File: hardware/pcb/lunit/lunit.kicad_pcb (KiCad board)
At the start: 4 copper layers, 62.2 x 21.6 mm, 41 parts, among them J1 BUS, J2 Input A, J3 Input B, J4 Control, J5 Flags, J6 Power, U7 74HC245, U8 74HC125

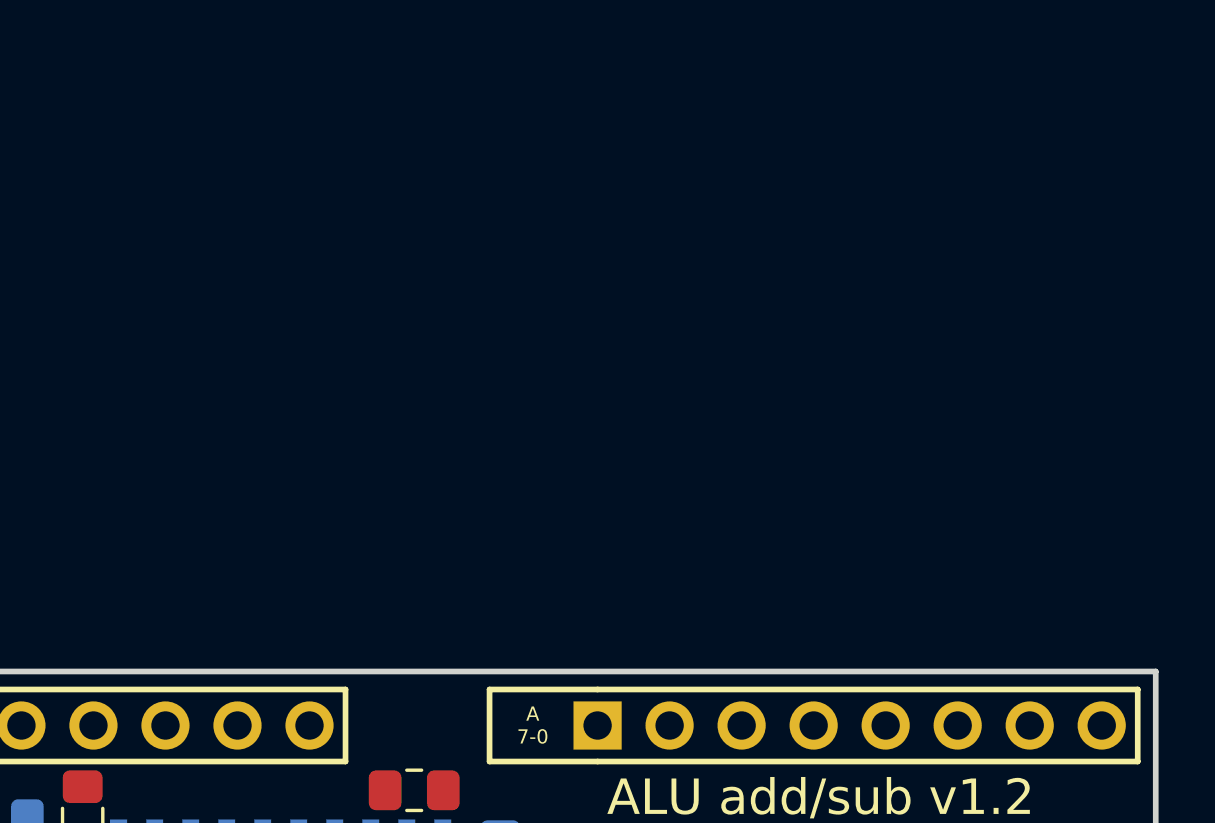
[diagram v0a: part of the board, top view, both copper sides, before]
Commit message: Add And/Or/Sel chips
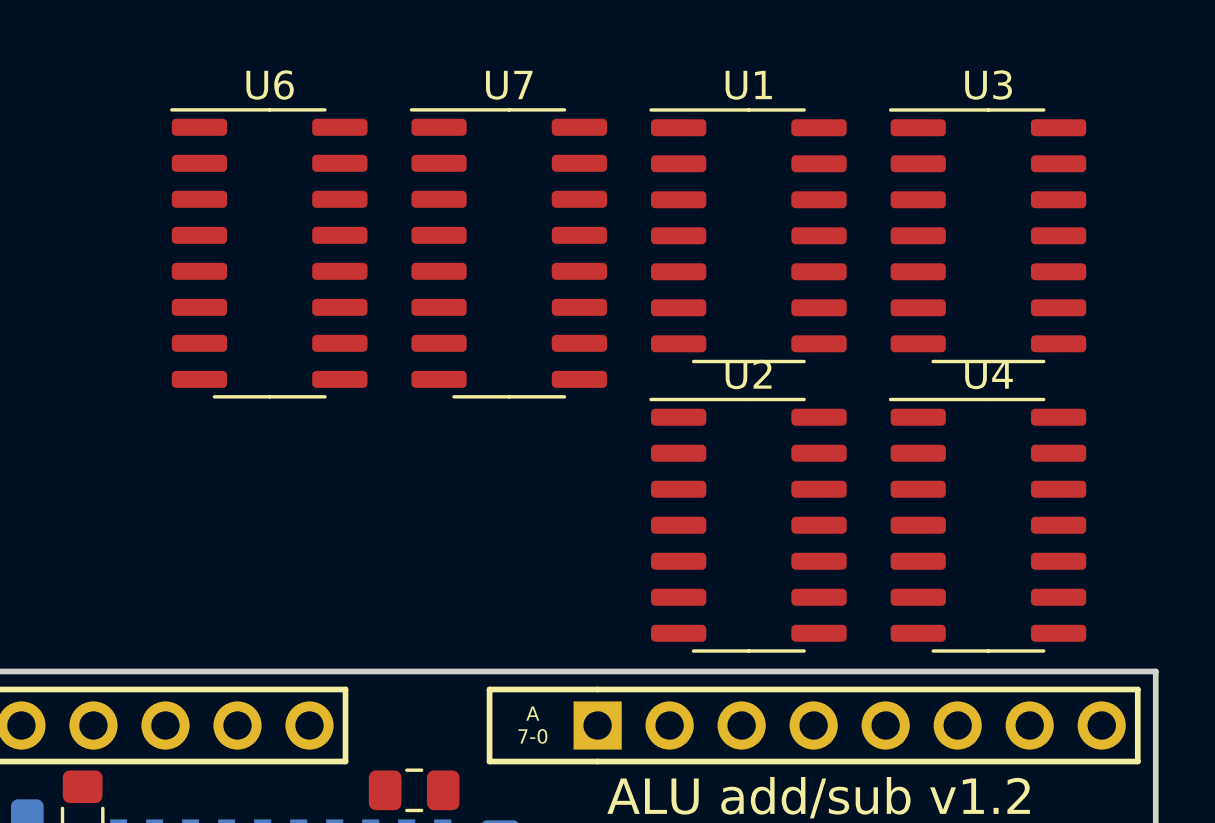
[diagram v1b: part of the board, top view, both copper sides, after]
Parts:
- added U1: 74HC08, Package_SO:SOIC-14_3.9x8.7mm_P1.27mm, F.Cu at (82.8, 20.8)
- added U2: 74HC08, Package_SO:SOIC-14_3.9x8.7mm_P1.27mm, F.Cu at (82.8, 31.0)
- added U3: 74HC32, Package_SO:SOIC-14_3.9x8.7mm_P1.27mm, F.Cu at (91.3, 20.8)
- added U4: 74HC32, Package_SO:SOIC-14_3.9x8.7mm_P1.27mm, F.Cu at (91.3, 31.0)
- added U6: 74HC157, Package_SO:SOIC-16_3.9x9.9mm_P1.27mm, F.Cu at (65.9, 21.4)
- added U7: 74HC157, Package_SO:SOIC-16_3.9x9.9mm_P1.27mm, F.Cu at (74.4, 21.4)
- renumbered D0 to D1, D11 to D10, D12 to D11, D1 to D2, D2 to D3, D3 to D4, D4 to D5, D5 to D6, D6 to D7, D7 to D8, D8 to D9, J6 to J1, J4 to J2, J1 to J3, J2 to J4, J3 to J6, R0 to R1, R11 to R10, R14 to R11, R1 to R2, R2 to R3, R3 to R4, R4 to R5, R5 to R6, R6 to R7, R7 to R8, R8 to R9, U8 to U5, U7 to U8
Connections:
- net ADD_SUB renamed AND_OR
- J4 pad 1: (no net) -> A7
- J4 pad 2: (no net) -> A6
- J4 pad 3: (no net) -> A5
- J4 pad 4: (no net) -> A4
- J4 pad 5: (no net) -> A3
- J4 pad 6: (no net) -> A2
- J4 pad 7: (no net) -> A1
- J4 pad 8: (no net) -> A0
- J6 pad 1: (no net) -> B7
- J6 pad 2: (no net) -> B6
- J6 pad 3: (no net) -> B5
- J6 pad 4: (no net) -> B4
- J6 pad 5: (no net) -> B3
- J6 pad 6: (no net) -> B2
- J6 pad 7: (no net) -> B1
- J6 pad 8: (no net) -> B0

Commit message: Place the chips
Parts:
- D10: value SUB -> OR
- U3, U4: moved to B.Cu
- moved U3 27.8 mm to (80.3, 46.4)
- moved U1 25.6 mm to (80.4, 46.4), turned to 180 degrees
- moved U6 24.8 mm to (55.9, 44.1), turned to 90 degrees
- moved U7 23.3 mm to (69.1, 44.1), turned to 90 degrees
- moved U2 17.3 mm to (90.9, 46.4), turned to 180 degrees
- moved U4 15.3 mm to (90.9, 46.4)
- moved C6 9.71 mm to (49.7, 42.3)
- moved C8 8.36 mm to (62.9, 42.3), turned to 270 degrees
- moved D3 2.03 mm to (66.8, 50.7)
- moved D11 2.03 mm to (52.8, 50.7)
- moved D4 2.03 mm to (64.9, 50.7)
- moved D6 2.03 mm to (61.1, 50.7)
- moved D7 2.03 mm to (59.2, 50.7)
- moved D8 2.03 mm to (57.3, 50.7)
- moved D1 2.03 mm to (70.6, 50.7)
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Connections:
- net SUM0 renamed RES0
- net SUM1 renamed RES1
- net SUM2 renamed RES2
- net SUM3 renamed RES3
- net SUM4 renamed RES4
- net SUM5 renamed RES5
- net SUM6 renamed RES6
- net SUM7 renamed RES7
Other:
- board text added: "/ / / Z"
- board text added: "ALU and/or v1.0"
- board text removed: "6502"
- board text removed: "ALU add/sub v1.2"
- board text removed: "CI V CO Z"
- board text removed: "Z80"

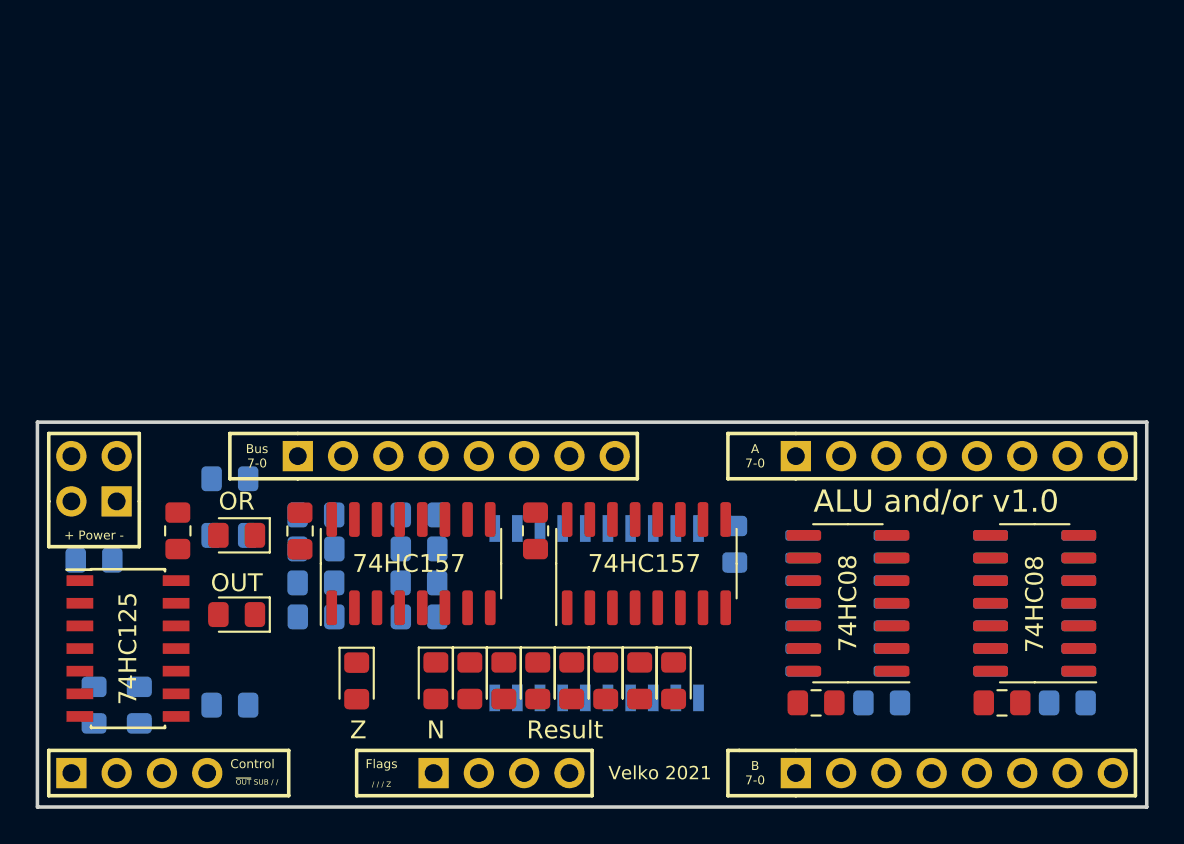
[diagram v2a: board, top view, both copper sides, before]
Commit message: Routed function part
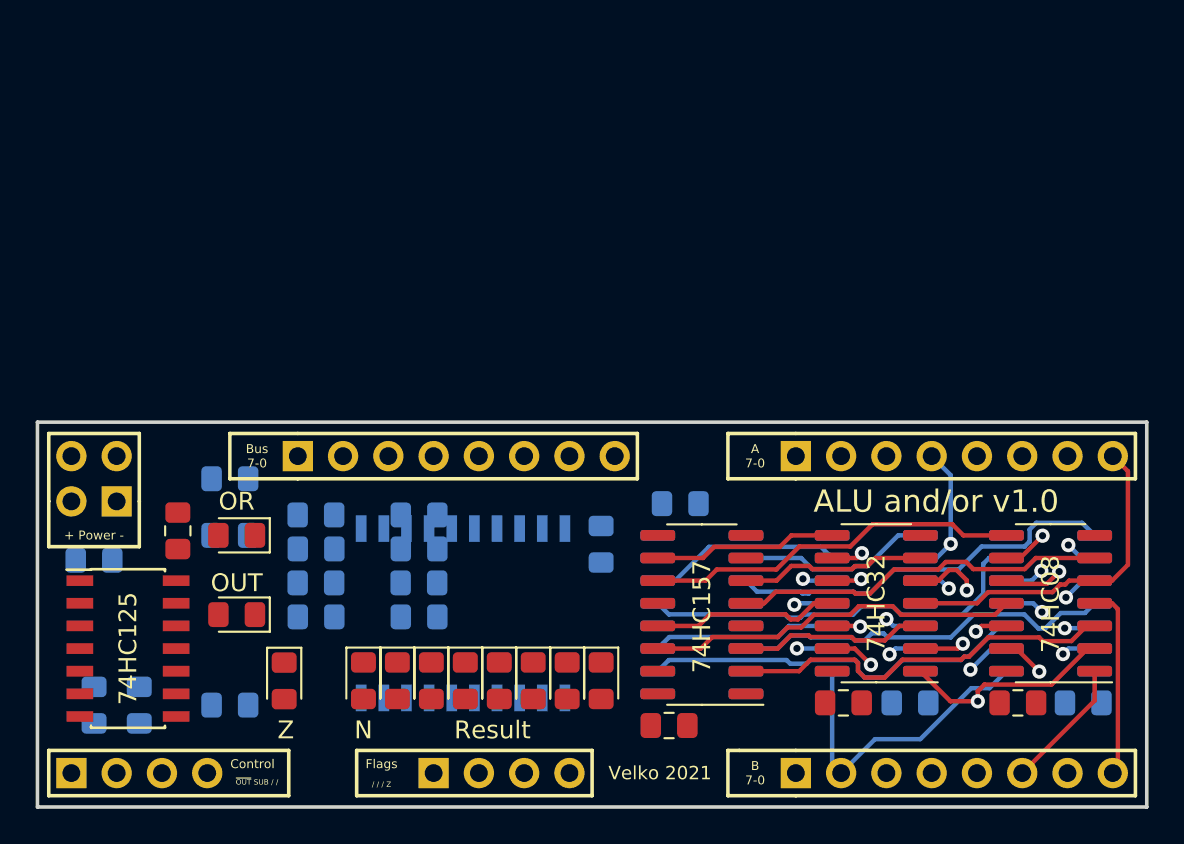
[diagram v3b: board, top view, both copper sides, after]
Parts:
- C6, U1, U6: moved to B.Cu
- U4: moved to F.Cu
- moved C6 21.4 mm to (71.0, 40.8), turned to 0 degrees
- moved U6 16.6 mm to (72.2, 47.0), turned to 180 degrees
- moved C8 13.2 mm to (70.4, 53.2), turned to 0 degrees
- moved U3 11.4 mm to (91.8, 46.4)
- moved U4 8.89 mm to (82.0, 46.4), turned to 180 degrees
- moved C2 7.49 mm to (66.5, 43.0)
- moved U8 7.49 mm to (58.8, 46.9)
- moved U7 4.22 mm to (72.2, 47.0), turned to 180 degrees
- moved D3 4.06 mm to (62.7, 50.7)
- moved D4 4.06 mm to (60.8, 50.7)
- moved D11 4.06 mm to (48.8, 50.7)
- moved D5 4.06 mm to (58.9, 50.7)
- moved D6 4.06 mm to (57.0, 50.7)
- moved D7 4.06 mm to (55.1, 50.7)
- moved D8 4.06 mm to (53.2, 50.7)
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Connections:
- J2 pad 3: (no net) -> Net-(J2-Pad3)
- J2 pad 4: (no net) -> Net-(J2-Pad4)
- J5 pad 1: (no net) -> Net-(J5-Pad1)
- J5 pad 2: (no net) -> Net-(J5-Pad2)
- J5 pad 3: (no net) -> Net-(J5-Pad3)
- U1 pad 1: A7 -> B6
- U1 pad 10: B5 -> B4
- U1 pad 11: AND4 -> AND5
- U1 pad 12: A4 -> A5
- U1 pad 13: B4 -> B5
- U1 pad 2: B7 -> A6
- U1 pad 3: AND7 -> AND6
- U1 pad 4: A6 -> B7
- U1 pad 5: B6 -> A7
- U1 pad 6: AND6 -> AND7
- U1 pad 8: AND5 -> AND4
- U1 pad 9: A5 -> A4
- U2 pad 1: A3 -> B2
- U2 pad 11: AND0 -> AND3
- U2 pad 12: A0 -> A3
- U2 pad 13: B0 -> B3
- U2 pad 2: B3 -> A2
- U2 pad 3: AND3 -> AND2
- U2 pad 4: A2 -> B0
- U2 pad 5: B2 -> A0
- U2 pad 6: AND2 -> AND0
- U3 pad 1: A7 -> B6
- U3 pad 10: B5 -> B4
- U3 pad 11: OR4 -> OR5
- U3 pad 12: A4 -> A5
- U3 pad 13: B4 -> B5
- U3 pad 2: B7 -> A6
- U3 pad 3: OR7 -> OR6
- U3 pad 4: A6 -> B7
- U3 pad 5: B6 -> A7
- U3 pad 6: OR6 -> OR7
- U3 pad 8: OR5 -> OR4
- U3 pad 9: A5 -> A4
- U4 pad 1: A3 -> A2
- U4 pad 11: OR0 -> OR3
- U4 pad 12: A0 -> A3
- U4 pad 13: B0 -> B3
- U4 pad 2: B3 -> B2
- U4 pad 3: OR3 -> OR2
- U4 pad 4: A2 -> A0
- U4 pad 5: B2 -> B0
- U4 pad 6: OR2 -> OR0
- U6 pad 10: OR5 -> OR6
- U6 pad 11: AND5 -> AND6
- U6 pad 12: RES4 -> RES7
- U6 pad 13: OR4 -> OR7
- U6 pad 14: AND4 -> AND7
- U6 pad 2: AND7 -> AND4
- U6 pad 3: OR7 -> OR4
- U6 pad 4: RES7 -> RES4
- U6 pad 5: AND6 -> AND5
- U6 pad 6: OR6 -> OR5
- U6 pad 7: RES6 -> RES5
- U6 pad 9: RES5 -> RES6
- U7 pad 12: RES0 -> RES3
- U7 pad 13: OR0 -> OR3
- U7 pad 14: AND0 -> AND3
- U7 pad 2: AND3 -> AND2
- U7 pad 3: OR3 -> OR2
- U7 pad 4: RES3 -> RES2
- U7 pad 5: AND2 -> AND0
- U7 pad 6: OR2 -> OR0
- U7 pad 7: RES2 -> RES0
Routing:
- net B0: track 0.00 -> 31.1 mm, vias 0 -> 1
- net B1: track 0.00 -> 29.5 mm, vias 0 -> 2
- net B7: track 0.00 -> 28.4 mm, vias 0 -> 2
- net A6: track 0.00 -> 26.9 mm, vias 0 -> 2
- net A2: track 0.00 -> 26.8 mm, vias 0 -> 1
- net A7: track 0.00 -> 25.2 mm, vias 0 -> 2
- net A5: track 0.00 -> 23.2 mm, vias 0 -> 2
- net OR7: track 0.00 -> 22.6 mm
- net OR4: track 0.00 -> 22.3 mm
- net AND2: track 0.00 -> 21.9 mm
- net OR6: track 0.00 -> 21.9 mm
- net B4: track 0.00 -> 21.8 mm, vias 0 -> 2
- net B5: track 0.00 -> 21.8 mm, vias 0 -> 2
- net OR5: track 0.00 -> 21.7 mm
- net B3: track 0.00 -> 21.3 mm, vias 0 -> 2
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
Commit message: Route the rest
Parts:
- R1, R2, R3, R4, R5, R6, R7, R8: moved to F.Cu
- moved D10 17.6 mm to (60.6, 52.6)
- moved R10 13.5 mm to (47.8, 52.7)
- moved R1 10.8 mm to (65.0, 47.9), turned to 270 degrees
- moved R11 10.1 mm to (47.9, 42.2), turned to 90 degrees
- moved R5 9.44 mm to (57.4, 47.9), turned to 270 degrees
- moved D9 9.14 mm to (53.3, 52.6)
- moved D7 8.66 mm to (53.6, 42.2)
- moved D1 8.64 mm to (65.0, 42.2)
- moved D2 8.64 mm to (63.1, 42.2)
- moved D3 8.64 mm to (61.2, 42.2)
- moved D4 8.64 mm to (59.3, 42.2)
- moved D5 8.64 mm to (57.4, 42.2)
- moved D6 8.64 mm to (55.5, 42.2)
- moved D8 8.64 mm to (51.7, 42.2)
- moved D11 8.58 mm to (47.9, 42.2)
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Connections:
- D1 pad 1: Net-(D1-Pad1) -> GND
- D1 pad 2: RES0 -> Net-(D1-Pad2)
- D2 pad 1: Net-(D2-Pad1) -> GND
- D2 pad 2: RES1 -> Net-(D2-Pad2)
- D3 pad 1: Net-(D3-Pad1) -> GND
- D3 pad 2: RES2 -> Net-(D3-Pad2)
- D4 pad 1: Net-(D4-Pad1) -> GND
- D4 pad 2: RES3 -> Net-(D4-Pad2)
- D5 pad 1: Net-(D5-Pad1) -> GND
- D5 pad 2: RES4 -> Net-(D5-Pad2)
- D6 pad 1: Net-(D6-Pad1) -> GND
- D6 pad 2: RES5 -> Net-(D6-Pad2)
- D7 pad 1: Net-(D7-Pad1) -> GND
- D7 pad 2: RES6 -> Net-(D7-Pad2)
- D8 pad 1: Net-(D8-Pad1) -> GND
- D8 pad 2: RES7 -> Net-(D8-Pad2)
- R1 pad 1: GND -> Net-(D1-Pad2)
- R1 pad 2: Net-(D1-Pad1) -> RES0
- R2 pad 1: GND -> Net-(D2-Pad2)
- R2 pad 2: Net-(D2-Pad1) -> RES1
- R3 pad 1: GND -> Net-(D3-Pad2)
- R3 pad 2: Net-(D3-Pad1) -> RES2
- R4 pad 1: GND -> Net-(D4-Pad2)
- R4 pad 2: Net-(D4-Pad1) -> RES3
- R5 pad 1: GND -> Net-(D5-Pad2)
- R5 pad 2: Net-(D5-Pad1) -> RES4
- R6 pad 1: GND -> Net-(D6-Pad2)
- R6 pad 2: Net-(D6-Pad1) -> RES5
- R7 pad 1: GND -> Net-(D7-Pad2)
- R7 pad 2: Net-(D7-Pad1) -> RES6
- R8 pad 1: GND -> Net-(D8-Pad2)
- R8 pad 2: Net-(D8-Pad1) -> RES7
- U5 pad 1: (no net) -> VCC
- U5 pad 11: (no net) -> Net-(U5-Pad11)
- U5 pad 12: (no net) -> VCC
- U5 pad 13: (no net) -> VCC
- U5 pad 2: (no net) -> VCC
- U5 pad 3: (no net) -> Net-(U5-Pad3)
- U5 pad 4: (no net) -> VCC
- U5 pad 5: (no net) -> VCC
- U5 pad 6: (no net) -> Net-(U5-Pad6)
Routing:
- net AND_OR: track 0.00 -> 55.7 mm, vias 0 -> 3
- net ~OUT~: track 0.00 -> 48.7 mm, vias 0 -> 2
- net GND: track 0.00 -> 47.2 mm, vias 0 -> 16
- net VCC: track 0.00 -> 42.1 mm, vias 0 -> 7
- net RES7: track 0.00 -> 26.8 mm, vias 0 -> 2
- net RES5: track 0.00 -> 23.5 mm, vias 0 -> 1
- net RES4: track 0.00 -> 22.4 mm, vias 0 -> 1
- net ZIN: track 0.00 -> 22.0 mm
- net RES6: track 0.00 -> 20.1 mm, vias 0 -> 1
- net RES2: track 0.00 -> 17.6 mm, vias 0 -> 2
- net RES0: track 0.00 -> 16.6 mm, vias 0 -> 1
- net Net-(D10-Pad1): track 0.00 -> 16.3 mm, vias 0 -> 1
- net RES1: track 0.00 -> 14.9 mm, vias 0 -> 1
- net RES3: track 0.00 -> 14.8 mm, vias 0 -> 2
- net Net-(D11-Pad2): track 0.00 -> 14.7 mm
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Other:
- board text removed: "LED resistors"
